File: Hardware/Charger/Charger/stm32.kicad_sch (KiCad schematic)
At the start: 43 parts, among them J301 Conn_01x04_Socket, J302 Conn_02x03_Counter_Clockwise, SW301 SW_Push, SW302 SW_Push, U301 TCAN1042VDRQ1, U302 STM32G473CCTx, U303 MAX7221xWG, U304 CC56-12SEKWA, U50 LTV-356T, Y301 48 MHz

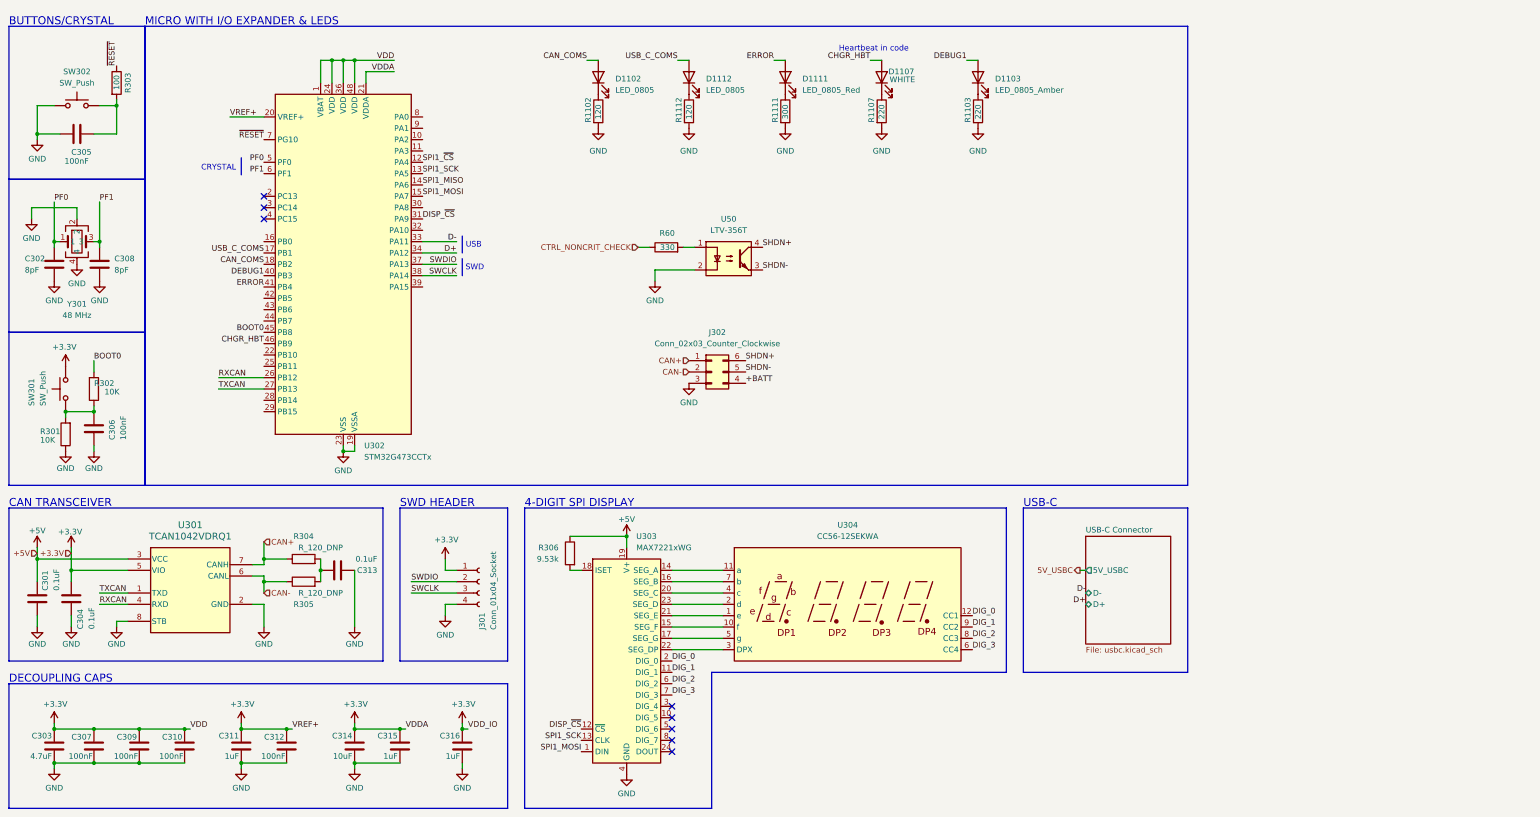
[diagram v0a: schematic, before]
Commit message: built charger schematic and added parts to layout
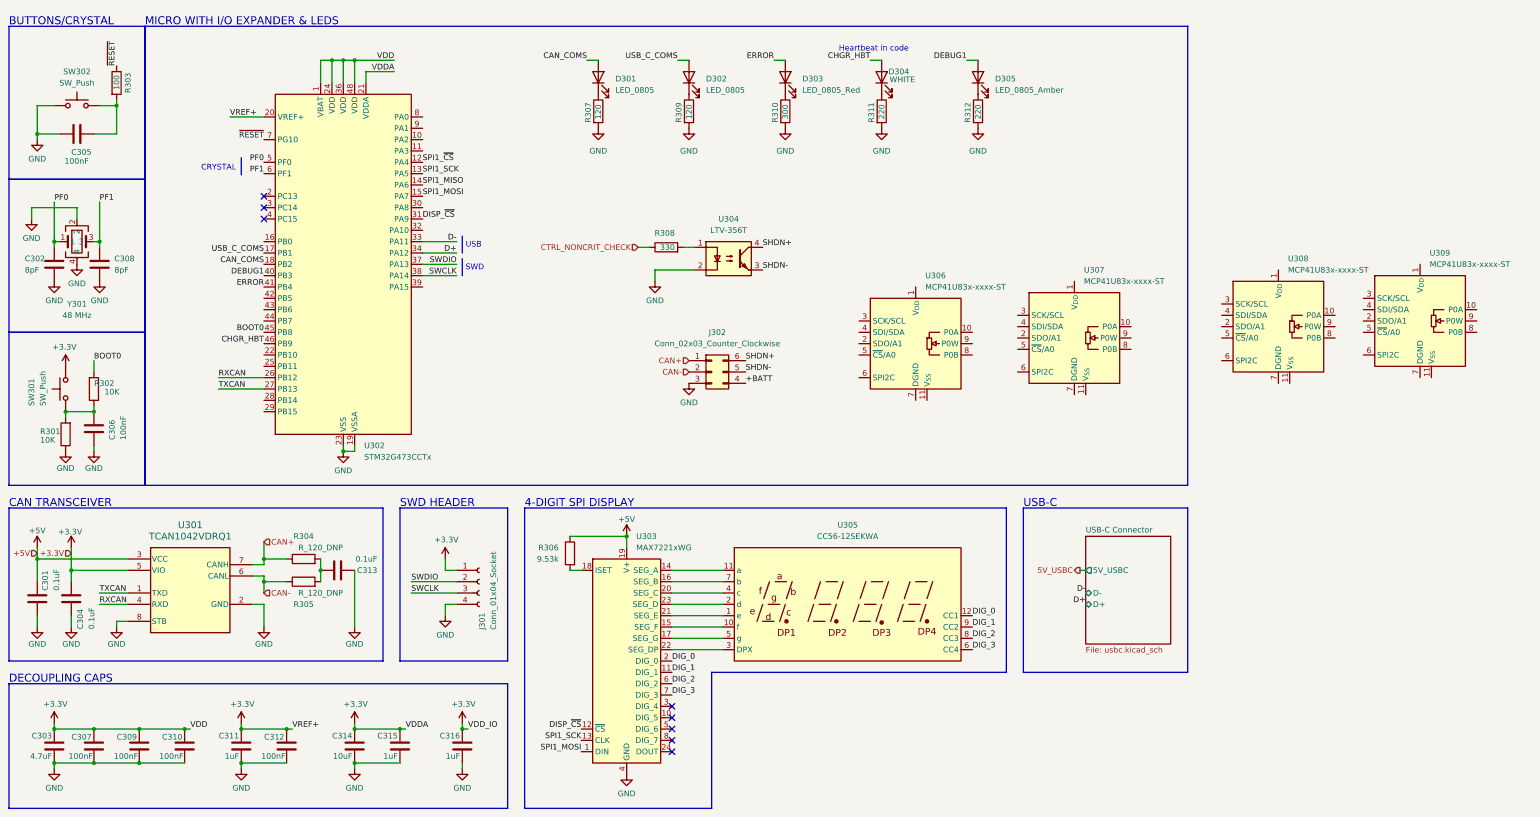
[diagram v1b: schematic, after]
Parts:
- added U306, U307, U308, U309: MCP41U83x-xxxx-ST, Package_SO:TSSOP-14_4.4x5mm_P0.65mm, symbol Potentiometer_Digital:MCP41U83x-xxxx-ST
- C301, C302, C303, C304, C306, C307, C308, C309, C310, C311, C312, C313, C314, C315, C316: footprint footprints:C_0603_1608Metric -> Capacitor_SMD:C_0603_1608Metric
- D301: renamed from D1102; footprint footprints:LED_0805_OEM -> LED_SMD:LED_0805_2012Metric
- D302: renamed from D1112; footprint footprints:LED_0805_OEM -> LED_SMD:LED_0805_2012Metric
- D303: renamed from D1111; footprint footprints:LED_0805_OEM -> LED_SMD:LED_0805_2012Metric
- D305: renamed from D1103; footprint footprints:LED_0805_OEM -> LED_SMD:LED_0805_2012Metric
- R301, R302, R303, R304, R305, R306: footprint footprints:R_0603_1608Metric -> Resistor_SMD:R_0603_1608Metric
- R307: renamed from R1102; footprint OEM:R_0603_1608Metric -> Resistor_SMD:R_0603_1608Metric
- R308: renamed from R60; footprint footprints:R_0603_1608Metric -> Resistor_SMD:R_0603_1608Metric
- R309: renamed from R1112; footprint OEM:R_0603_1608Metric -> Resistor_SMD:R_0603_1608Metric
- R310: renamed from R1111; footprint OEM:R_0603_1608Metric -> Resistor_SMD:R_0603_1608Metric
- R311: renamed from R1107; footprint OEM:R_0603_1608Metric -> Resistor_SMD:R_0603_1608Metric
- R312: renamed from R1103; footprint OEM:R_0603_1608Metric -> Resistor_SMD:R_0603_1608Metric
- Y301: footprint footprints:Crystal_SMD_FA238 -> Crystal:Crystal_SMD_SeikoEpson_FA238-4Pin_3.2x2.5mm
- renumbered D1107 to D304, U50 to U304, U304 to U305

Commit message: Added: Contactor control, Voltage sense, I2C comms for oled screen, 3v3 and 5v converters, power switch
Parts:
- removed R306: 9.53k, Resistor_SMD:R_0603_1608Metric, symbol Device:R
- removed U303: MAX7221xWG, Package_SO:SOIC-24W_7.5x15.4mm_P1.27mm, symbol Driver_LED:MAX7221xWG
- removed U305: CC56-12SEKWA, Display_7Segment:CA56-12SEKWA, symbol Display_Character:CC56-12SEKWA
- removed U306, U307, U308, U309: MCP41U83x-xxxx-ST, Package_SO:TSSOP-14_4.4x5mm_P0.65mm, symbol Potentiometer_Digital:MCP41U83x-xxxx-ST
- added J9: Conn_01x04, symbol Connector_Generic:Conn_01x04
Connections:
- net +3.3V: now also J9.2 (Pin_2)
- net GND: now also J9.1 (Pin_1)
- net DIGIPOT_~{CS}3: now reaches U302.10 (PA2)
- net DIGIPOT_~{CS}4: now reaches U302.11 (PA3)
- net VSENSE1: now reaches U302.28 (PB14)
- net CONTACT_CTRL: now reaches U302.29 (PB15)
- net DIN: now reaches U302.30 (PA8)
- net SCL: now reaches U302.43 (PB6)
- net SCL: now also J9.3 (Pin_3)
- net SDA: now reaches U302.44 (PB7)
- net SDA: now also J9.4 (Pin_4)
- net DIGIPOT_~{CS}1: now reaches U302.8 (PA0)
- net DIGIPOT_~{CS}2: now reaches U302.9 (PA1)
- net DISP_~{CS} renamed NO
- no-connect marks 8 -> 3
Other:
- note added: "OLED SCREEN"
- note removed: "4-DIGIT SPI DISPLAY"

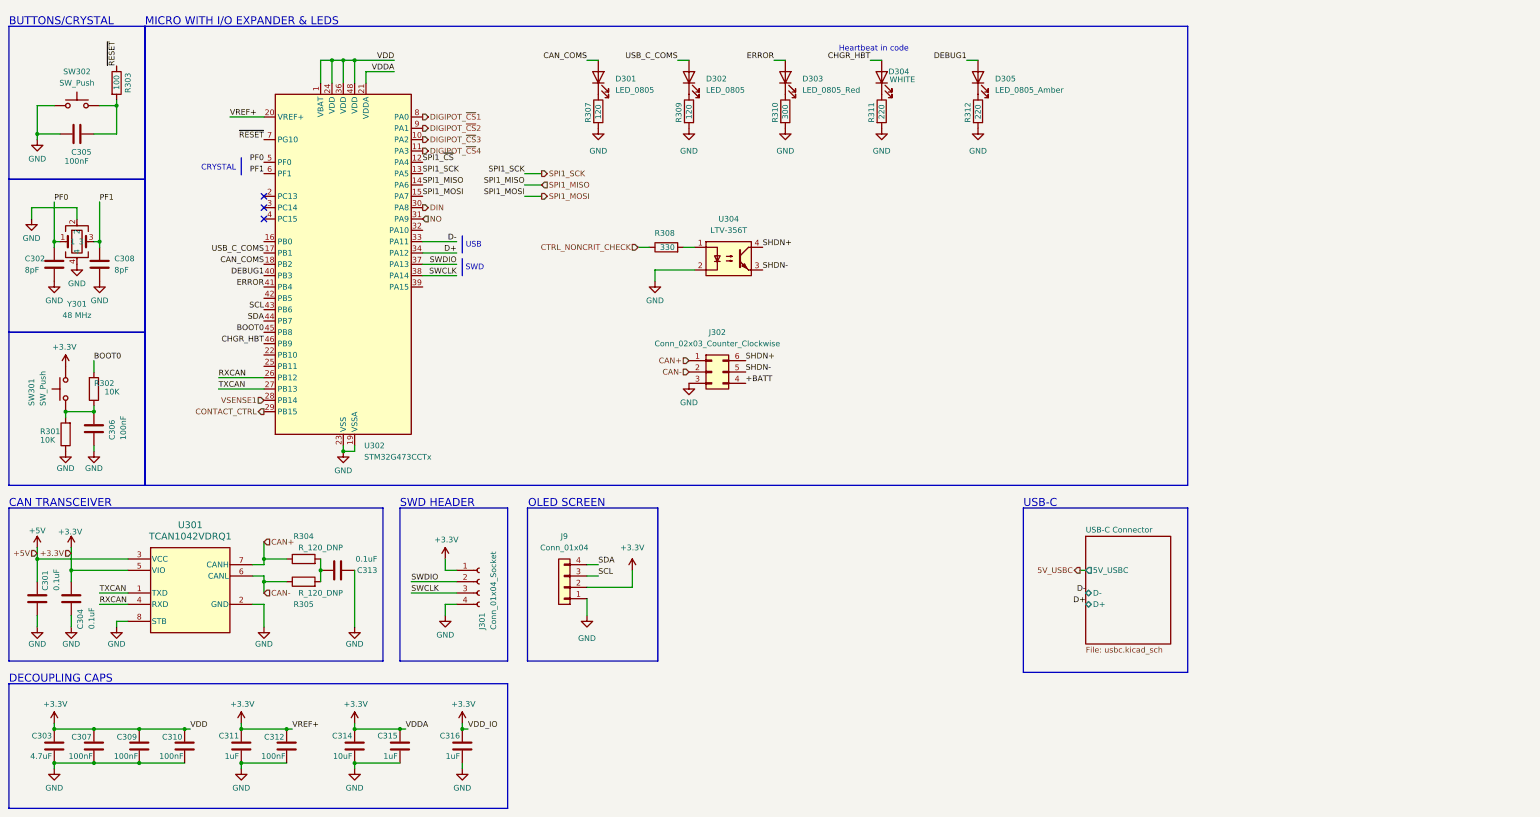
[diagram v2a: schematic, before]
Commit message: Few updates to connectors
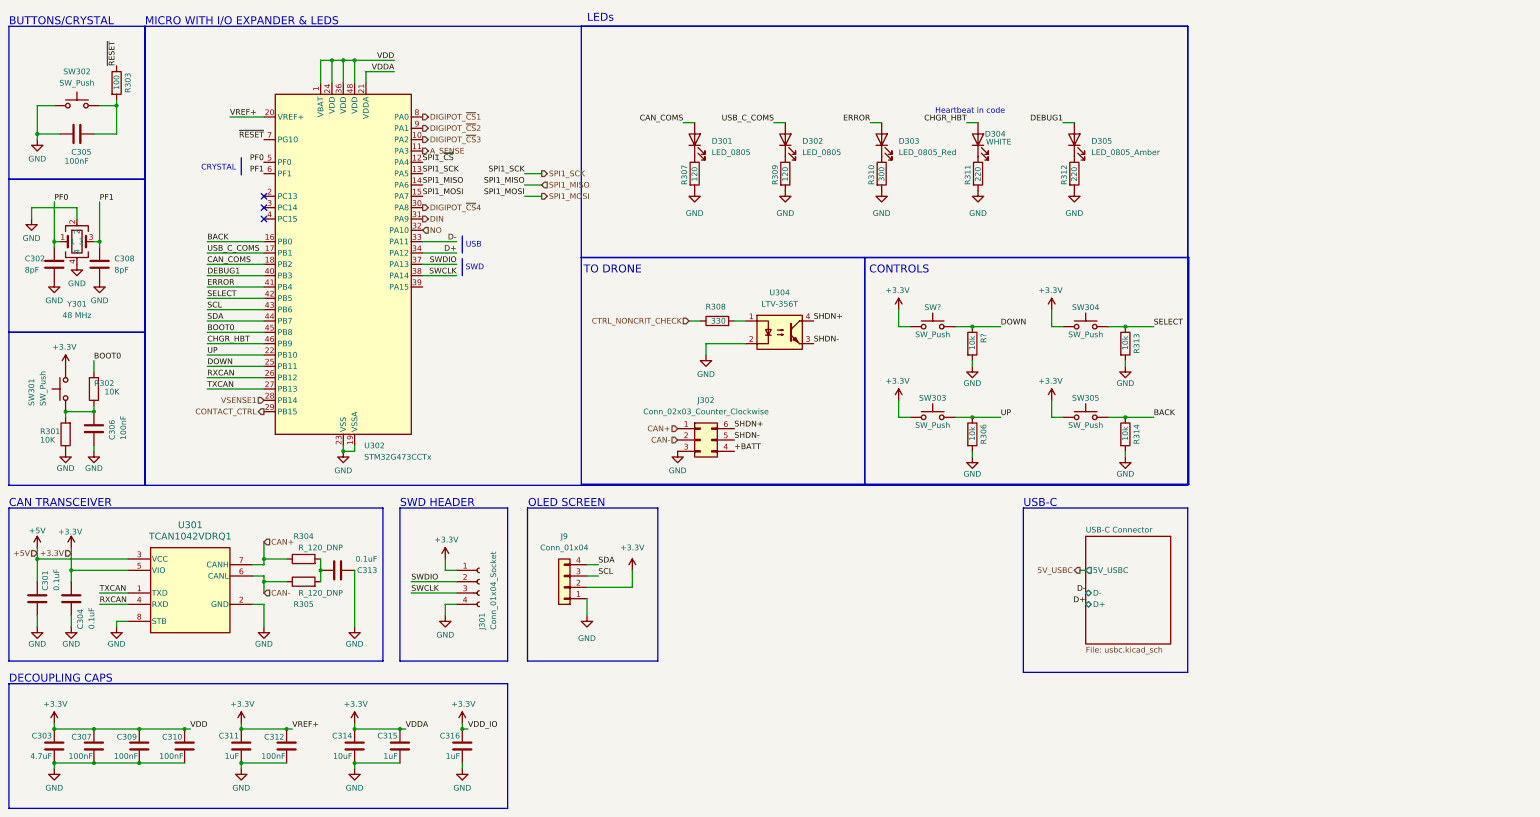
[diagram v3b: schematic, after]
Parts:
- added R306, R313, R314, R?: 10k, Resistor_SMD:R_0603_1608Metric, symbol formula:R_10K
- added SW303, SW304, SW305, SW?: SW_Push, Button_Switch_SMD:SW_Push_1P1T_NO_CK_KMR2, symbol Switch:SW_Push
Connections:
- net +3.3V: now also SW303.1, SW304.1, SW305.1, SW?.1
- net DIGIPOT_~{CS}4: now also U302.30 (PA8); no longer U302.11 (PA3)
- net DIN: now also U302.31 (PA9); no longer U302.30 (PA8)
- net GND: now also R306.2, R313.2, R314.2, R?.2
- net NO: now also U302.32 (PA10); no longer U302.31 (PA9)
- net BACK: now reaches U302.16 (PB0)
- net BACK: now also R314.1, SW305.2
- net UP: now reaches U302.22 (PB10)
- net UP: now also R306.1, SW303.2
- net DOWN: now reaches U302.25 (PB11)
- net DOWN: now also R?.1, SW?.2
- net SELECT: now reaches U302.42 (PB5)
- net SELECT: now also R313.1, SW304.2
- new net A_SENSE: U302.11 (PA3)
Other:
- note added: "CONTROLS"
- note added: "LEDs"
- note added: "TO DRONE"
- moved on the sheet: D301, D302, D303, D304, D305, J302, R307, R308, R309, R310, R311, R312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

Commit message: Completed PCB layout of charger
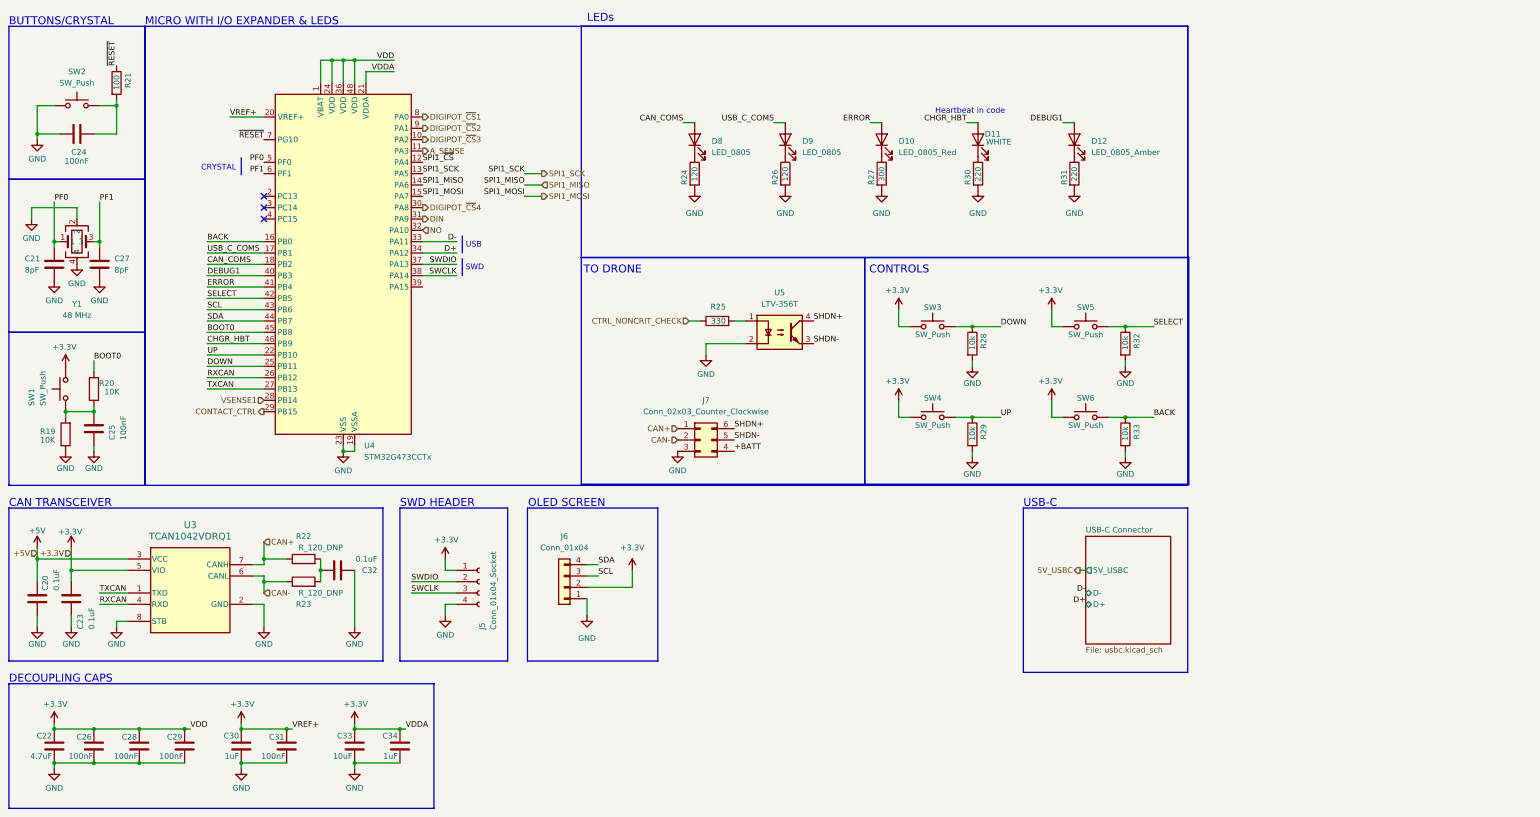
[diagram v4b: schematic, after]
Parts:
- removed C316: 1uF, Capacitor_SMD:C_0603_1608Metric, symbol formula:C_10uF
- J6: renamed from J9; footprint (none) -> Connector_PinHeader_2.54mm:PinHeader_1x04_P2.54mm_Vertical
- gave numbers to parts that had none: 2
- renumbered C301 to C20, C302 to C21, C303 to C22, C304 to C23, C305 to C24, C306 to C25, C307 to C26, C308 to C27, C309 to C28, C310 to C29, C311 to C30, C312 to C31, C313 to C32, C314 to C33, C315 to C34, D303 to D10, D304 to D11, D305 to D12, D301 to D8, D302 to D9, J301 to J5, J302 to J7, R301 to R19, R302 to R20, R303 to R21, R304 to R22, R305 to R23, R307 to R24, R308 to R25, R309 to R26, R310 to R27, R306 to R29, R311 to R30, R312 to R31, R313 to R32, R314 to R33, SW301 to SW1, SW302 to SW2, SW303 to SW4, SW304 to SW5, SW305 to SW6, U301 to U3, U302 to U4, U304 to U5, Y301 to Y1
